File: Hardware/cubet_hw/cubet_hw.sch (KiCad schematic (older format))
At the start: 99 parts, among them J1 USB_B_Micro, J2 Conn_01x32, J3 Conn_01x32, J4 Conn_01x32, J8 Conn_01x04_Male, Q1 A03400A, Q2 A03400A, Q3 A03400A, Q4 A03400A, Q5 A03400A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

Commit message: bootloader flashed, ready to program
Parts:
- removed JP1, JP2, JP3, JP4, JP5, JP6, JP7, JP8: SolderJumper_3_Bridged12, Jumper:SolderJumper-3_P1.3mm_Bridged12_RoundedPad1.0x1.5mm, symbol Jumper:SolderJumper_3_Bridged12
- removed R24, R25, R26, R27: 0R/NP, Resistor_SMD:R_0603_1608Metric_Pad1.05x0.95mm_HandSolder, symbol Device:R_Small
- added JP10, JP11, JP9: SolderJumper_3_Bridged12, Jumper:SolderJumper-3_P1.3mm_Bridged12_RoundedPad1.0x1.5mm, symbol Jumper:SolderJumper_3_Bridged12
- Q1, Q2, Q3, Q4, Q5, Q6, Q8, Q9: footprint Package_TO_SOT_SMD:SOT-23_Handsoldering -> Package_TO_SOT_SMD:SOT-23
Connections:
- net +5V: now also U4.10 (~SRCLR)
- net CTRL_ROW_0_SHIFT: now also R1.2
- net CTRL_ROW_1_SHIFT: now also R2.2
- net CTRL_ROW_2_SHIFT: now also R6.2
- net CTRL_ROW_3_SHIFT: now also R7.2
- net CTRL_ROW_4_SHIFT: now also R10.2
- net CTRL_ROW_5_SHIFT: now also R11.2
- net CTRL_ROW_6_SHIFT: now also R20.2
- net CTRL_ROW_7_SHIFT: now also R21.2
- net D+_UC: now also U2.34 (PA25)
- net D+_USB: no longer U2.34 (PA25)
- net GND: now also U4.13 (~OE)
- net MOSI: now also JP9.1 (A)
- net SCK: now also JP10.1 (A)
- net SHIFT_CLK: now also JP10.2 (C)
- net SHIFT_DATA: now also JP9.2 (C)
- net SHIFT_DATA_4: now also U10.14 (SER)
- net SHIFT_DATA_5: now also U11.14 (SER); no longer U10.14 (SER)
- net SHIFT_DATA_6: now also U12.14 (SER); no longer U11.14 (SER)
- net SHIFT_DATA_7: no longer U12.14 (SER)
- net SHIFT_LATCH: now also JP11.2 (C)
- net SS: now also JP11.1 (A)
- net LATCH_TCC: now reaches U2.29 (PA20)
- net LATCH_TCC: now also JP11.3 (B)
- net CTRL_ROW_0_UC: no longer names the net of U2.9 (PA04)
- net CTRL_ROW_1_UC: no longer names the net of U2.10 (PA05)
- net CTRL_ROW_2_UC: no longer names the net of U2.11 (PA06)
- net CTRL_ROW_3_UC: no longer names the net of U2.12 (PA07)
- net CTRL_ROW_4_UC: no longer names the net of U2.13 (PA08)
- net CTRL_ROW_5_UC: no longer names the net of U2.14 (PA09)
- net CTRL_ROW_6_UC: no longer names the net of U2.15 (PA10)
- net CTRL_ROW_7_UC: no longer names the net of U2.16 (PA11)
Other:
- note added: "Maybe the TCC can be used to latch the\nshift registers (DMA triggered), 100% Hardware\n"
- moved on the sheet: R31, R32

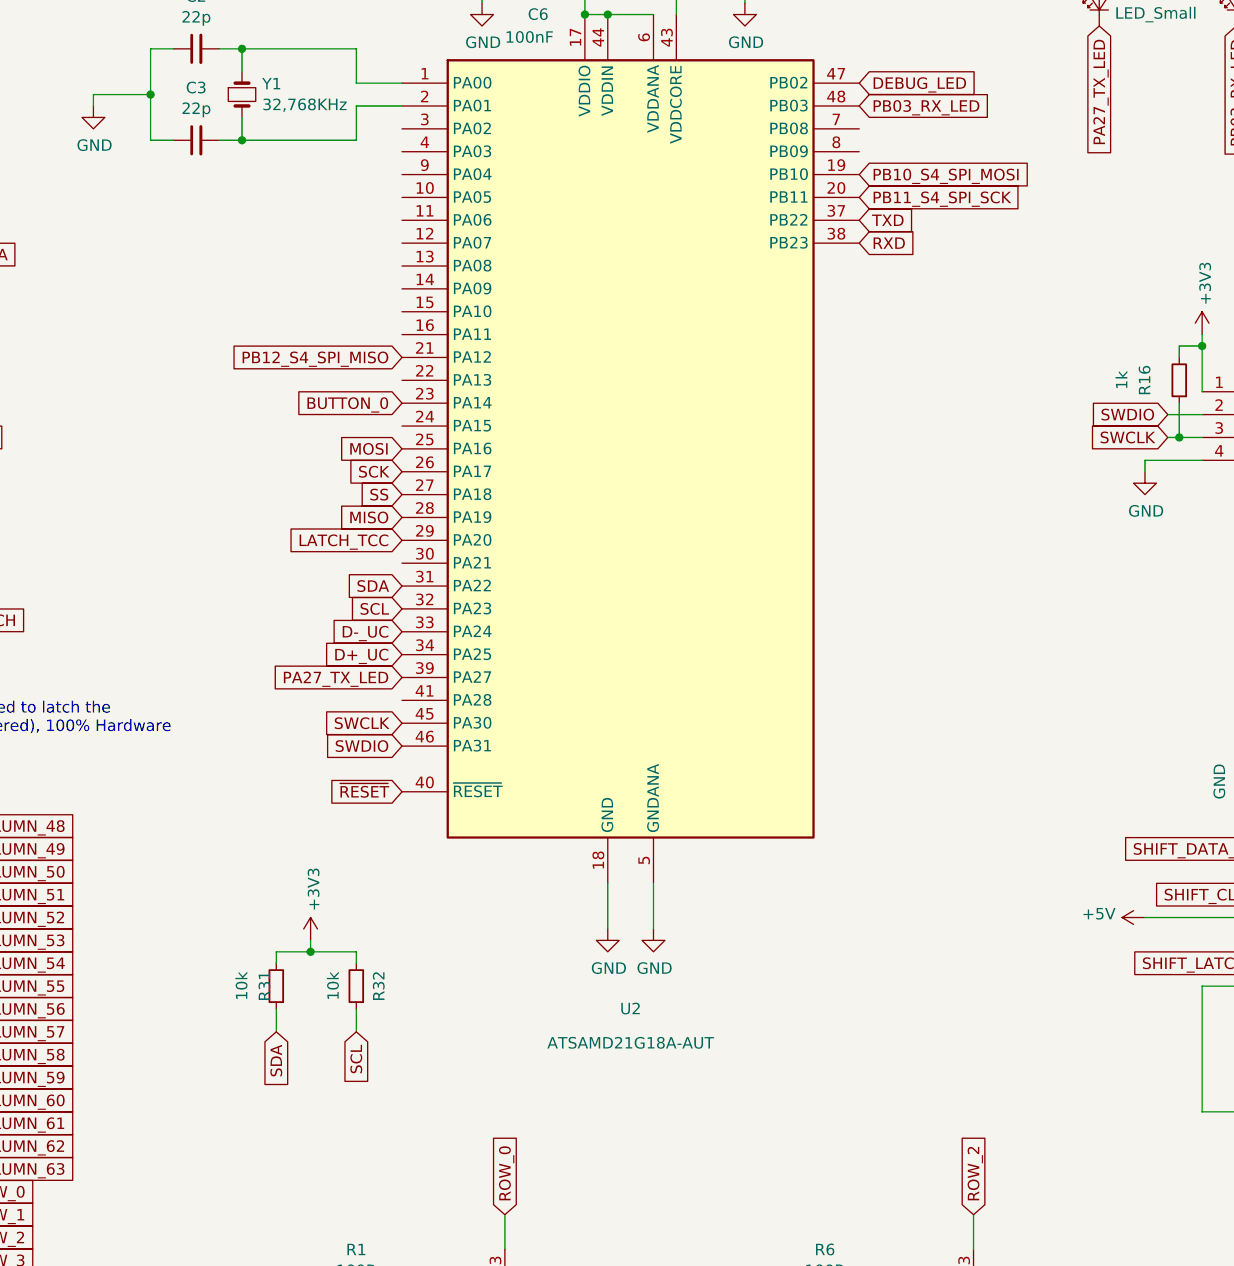
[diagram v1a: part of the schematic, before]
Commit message: First working SPI. First work in README
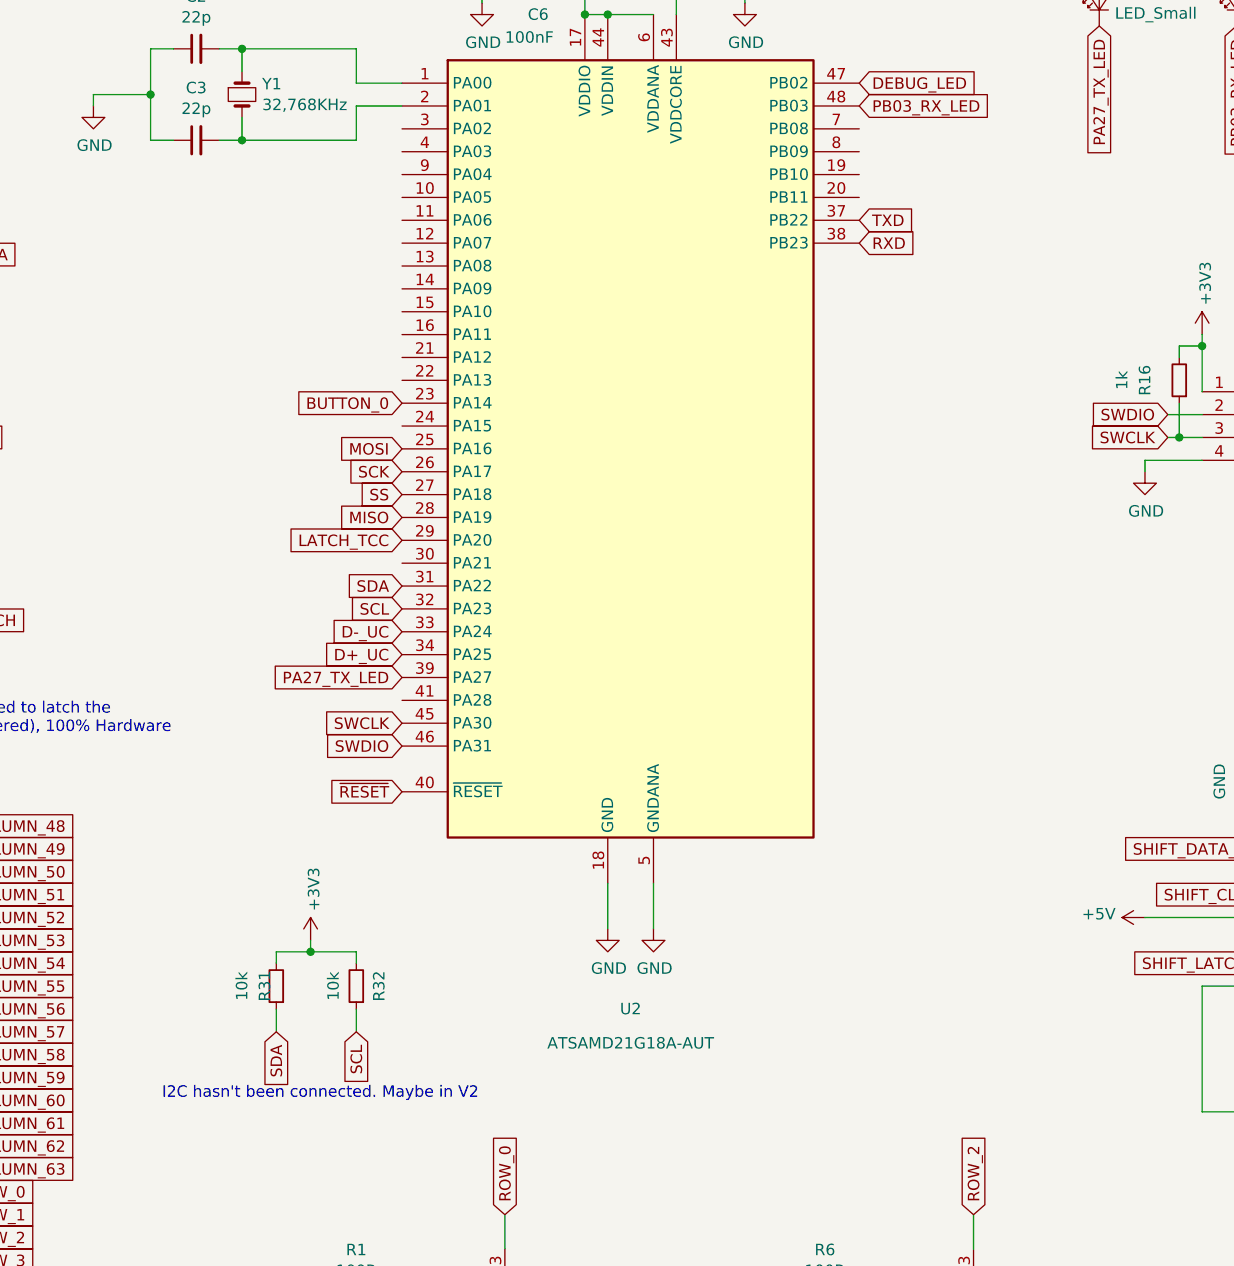
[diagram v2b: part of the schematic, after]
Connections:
- net PB10_S4_SPI_MOSI: no longer names the net of U2.19 (PB10)
- net PB11_S4_SPI_SCK: no longer names the net of U2.20 (PB11)
- net PB12_S4_SPI_MISO: no longer names the net of U2.21 (PA12)
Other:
- note added: "I2C hasn't been connected. Maybe in V2"
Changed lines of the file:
@@
 EESchema Schematic File Version 4
-LIBS:cubet_hw-cache
 EELAYER 30 0
 EELAYER END
@@
 Text GLabel 5350 4600 2    50   Input ~ 0
 RXD
-Text GLabel 5350 4300 2    50   Input ~ 0
-PB10_S4_SPI_MOSI
-Text GLabel 5350 4400 2    50   Input ~ 0
-PB11_S4_SPI_SCK
-Text GLabel 3350 5100 0    50   Input ~ 0
-PB12_S4_SPI_MISO
 Text GLabel 8400 3800 0    50   Input ~ 0
 BUTTON_0
@@
 Wire Wire Line
 	8950 10550 9150 10550
+Text Notes 2300 8350 0    50   ~ 0
+I2C hasn't been connected. Maybe in V2
 $EndSCHEMATC
